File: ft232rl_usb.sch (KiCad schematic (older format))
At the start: 23 parts, among them J1 USB, P10 CONN_2, U1 FT232RL, U2 LM1117

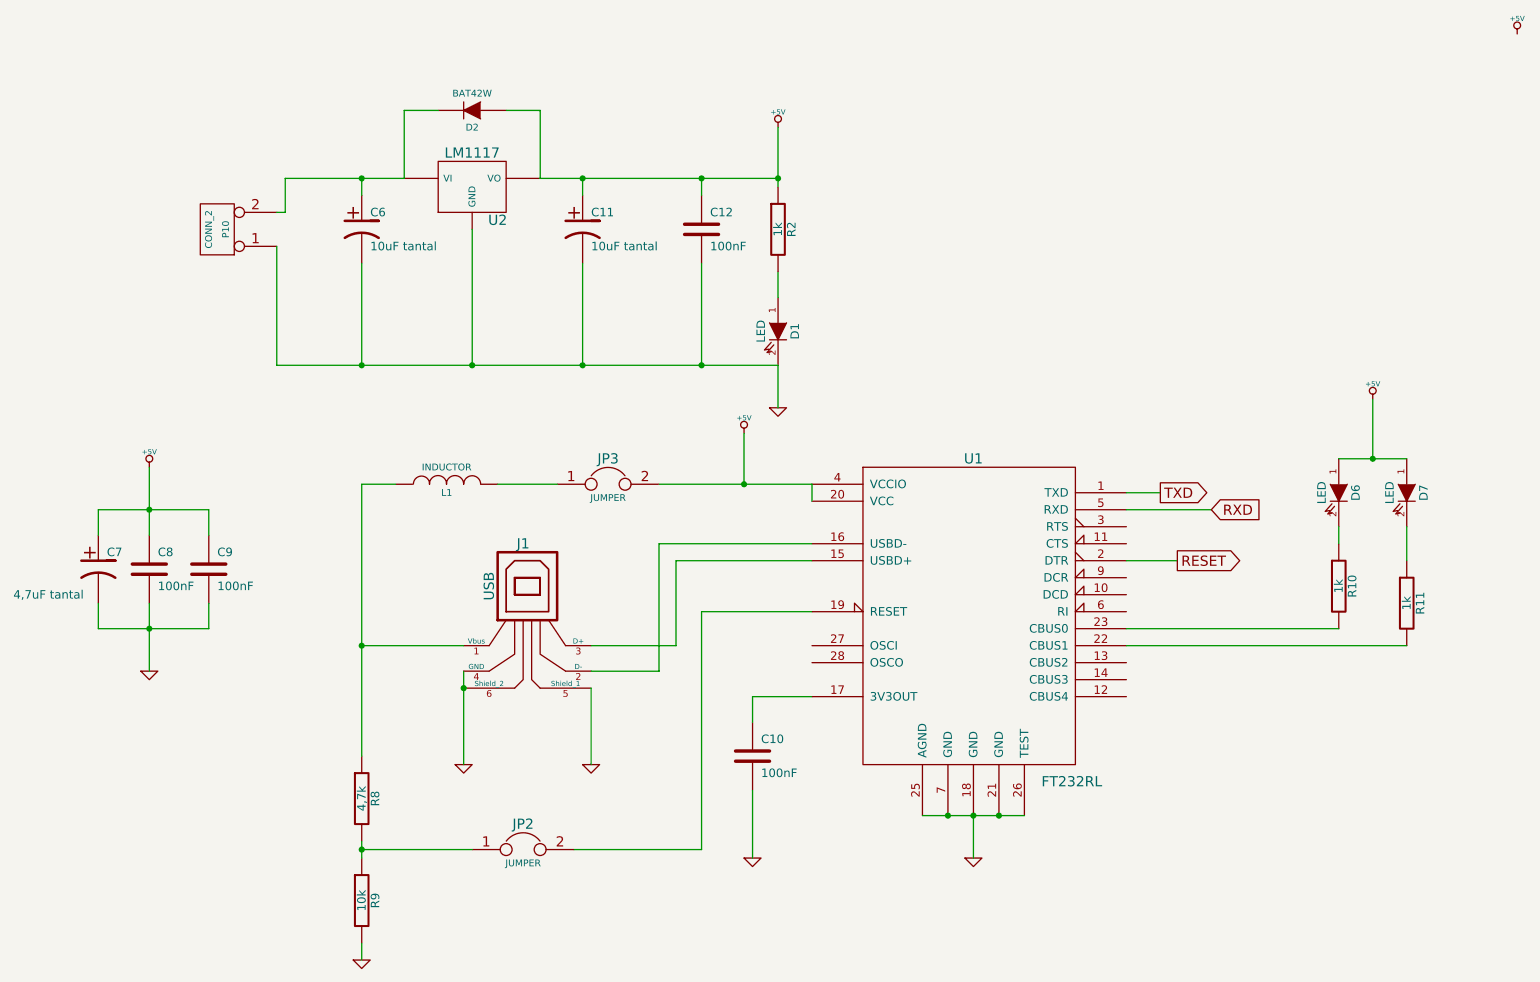
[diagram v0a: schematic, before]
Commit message: - Second version of the board - Added README for github
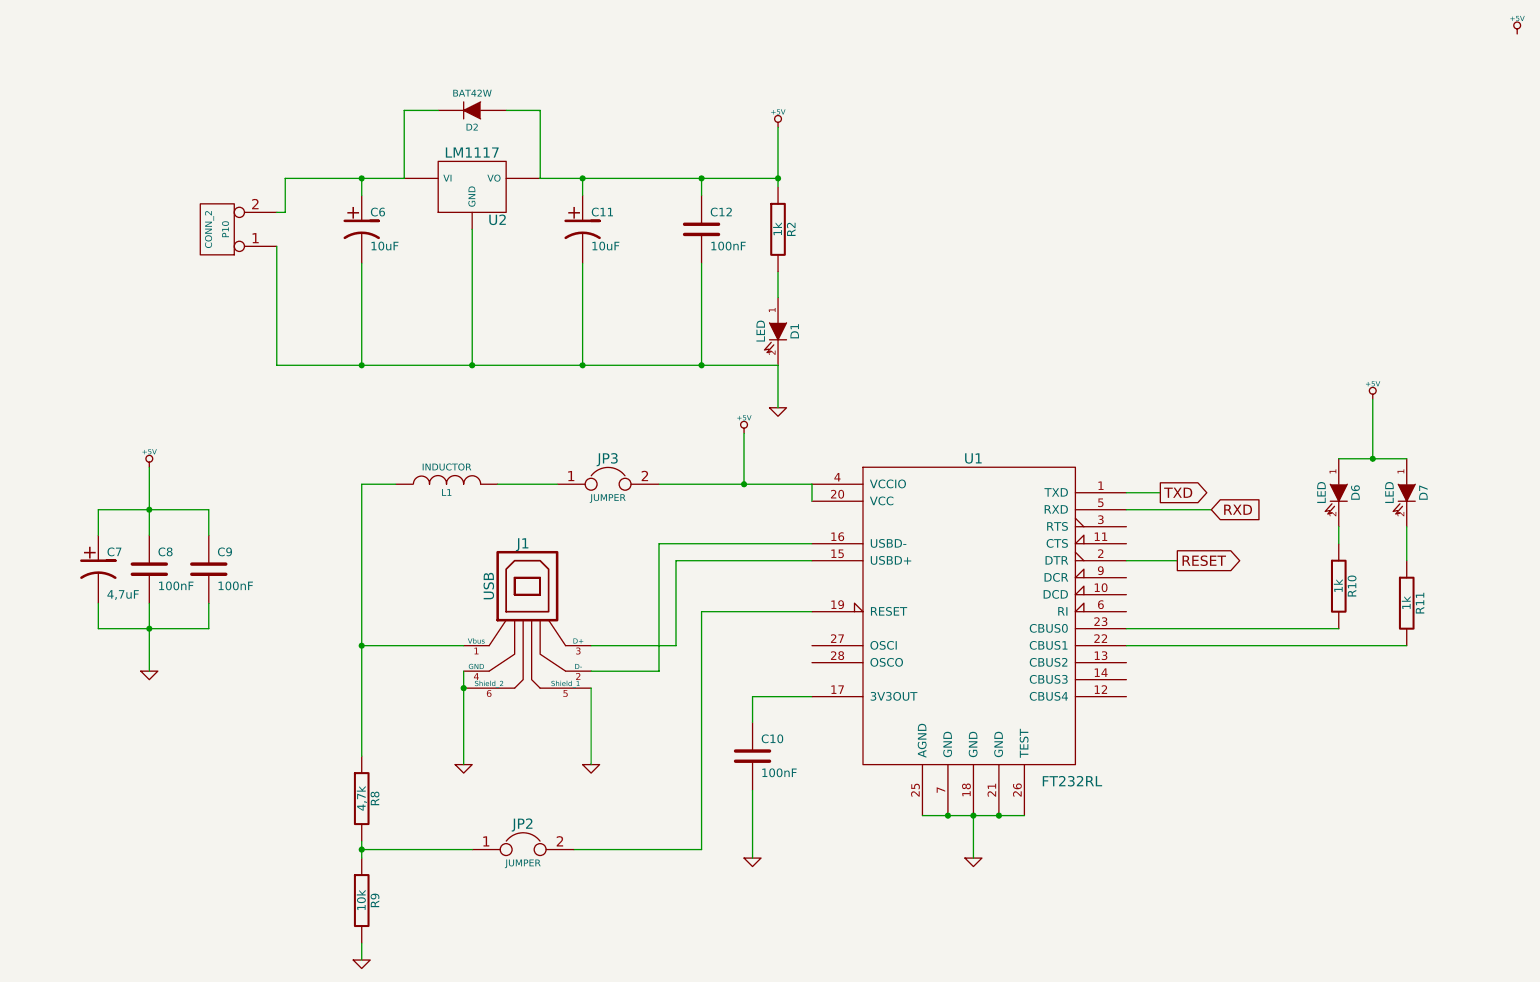
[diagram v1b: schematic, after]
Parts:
- C11, C6: value 10uF tantal -> 10uF
- C7: value 4,7uF tantal -> 4,7uF
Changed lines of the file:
@@
-EESchema Schematic File Version 2  date Sun 09 Dec 2012 11:53:08 PM CET
+EESchema Schematic File Version 2  date Thu 13 Dec 2012 04:01:05 PM CET
 LIBS:power
 LIBS:device
@@
 Sheet 2 2
 Title ""
-Date "9 dec 2012"
+Date "13 dec 2012"
 Rev ""
 Comp ""
@@
 $EndComp
 $Comp
-L GND #PWR013
+L GND #PWR015
 U 1 1 4F9D8FC2
 P 4700 4600
-F 0 "#PWR013" H 4700 4600 30  0001 C CNN
+F 0 "#PWR015" H 4700 4600 30  0001 C CNN
 F 1 "GND" H 4700 4530 30  0001 C CNN
 	1    4700 4600
@@
 P 1800 3450
 F 0 "C7" H 1850 3550 50  0000 L CNN
-F 1 "4,7uF tantal" H 1300 3300 50  0000 L CNN
+F 1 "4,7uF" H 1850 3300 50  0000 L CNN
 	1    1800 3450
 	1    0    0    -1
 $EndComp
 $Comp
-L GND #PWR014
+L GND #PWR016
 U 1 1 4F9D9229
 P 2100 4050
-F 0 "#PWR014" H 2100 4050 30  0001 C CNN
+F 0 "#PWR016" H 2100 4050 30  0001 C CNN
 F 1 "GND" H 2100 3980 30  0001 C CNN
 	1    2100 4050
@@
 $EndComp
 $Comp
-L +5V #PWR015
+L +5V #PWR017
 U 1 1 4F9D92D1
 P 2100 2850
-F 0 "#PWR015" H 2100 2940 20  0001 C CNN
+F 0 "#PWR017" H 2100 2940 20  0001 C CNN
 F 1 "+5V" H 2100 2940 30  0000 C CNN
 	1    2100 2850
@@
 $EndComp
 $Comp
-L +5V #PWR016
+L +5V #PWR018
 U 1 1 4F9D92E0
 P 5600 2650
-F 0 "#PWR016" H 5600 2740 20  0001 C CNN
+F 0 "#PWR018" H 5600 2740 20  0001 C CNN
 F 1 "+5V" H 5600 2740 30  0000 C CNN
 	1    5600 2650
@@
 $EndComp
 $Comp
-L GND #PWR017
+L GND #PWR019
 U 1 1 4F9D92EF
 P 3950 4600
-F 0 "#PWR017" H 3950 4600 30  0001 C CNN
+F 0 "#PWR019" H 3950 4600 30  0001 C CNN
 F 1 "GND" H 3950 4530 30  0001 C CNN
 	1    3950 4600
@@
 $EndComp
 $Comp
-L GND #PWR018
+L GND #PWR020
 U 1 1 4F9D9414
 P 6950 5150
-F 0 "#PWR018" H 6950 5150 30  0001 C CNN
+F 0 "#PWR020" H 6950 5150 30  0001 C CNN
 F 1 "GND" H 6950 5080 30  0001 C CNN
 	1    6950 5150
@@
 $EndComp
 $Comp
-L GND #PWR019
+L GND #PWR021
 U 1 1 4F9D9739
 P 3350 5750
-F 0 "#PWR019" H 3350 5750 30  0001 C CNN
+F 0 "#PWR021" H 3350 5750 30  0001 C CNN
 F 1 "GND" H 3350 5680 30  0001 C CNN
 	1    3350 5750
@@
 $EndComp
 $Comp
-L GND #PWR020
+L GND #PWR022
 U 1 1 4F9D9860
 P 5650 5150
-F 0 "#PWR020" H 5650 5150 30  0001 C CNN
+F 0 "#PWR022" H 5650 5150 30  0001 C CNN
 F 1 "GND" H 5650 5080 30  0001 C CNN
 	1    5650 5150
@@
 $EndComp
 $Comp
-L +5V #PWR021
+L +5V #PWR023
 U 1 1 4F9D9CC7
 P 9300 2450
-F 0 "#PWR021" H 9300 2540 20  0001 C CNN
+F 0 "#PWR023" H 9300 2540 20  0001 C CNN
 F 1 "+5V" H 9300 2540 30  0000 C CNN
 	1    9300 2450
@@
 P 3350 1450
 F 0 "C6" H 3400 1550 50  0000 L CNN
-F 1 "10uF tantal" H 3400 1350 50  0000 L CNN
+F 1 "10uF" H 3400 1350 50  0000 L CNN
 	1    3350 1450
 	1    0    0    -1
@@
 P 4650 1450
 F 0 "C11" H 4700 1550 50  0000 L CNN
-F 1 "10uF tantal" H 4700 1350 50  0000 L CNN
+F 1 "10uF" H 4700 1350 50  0000 L CNN
 	1    4650 1450
 	1    0    0    -1
@@
 Connection ~ 3350 3900
 Wire Wire Line
-	3350 4550 3350 3900
-Wire Wire Line
-	3350 3900 3350 2950
+	3350 2950 3350 4550
 Wire Wire Line
 	8150 3400 7850 3400
@@
 	9300 2800 9300 2450
 Wire Wire Line
-	9100 2800 9300 2800
-Wire Wire Line
-	9300 2800 9500 2800
+	9100 2800 9500 2800
 Wire Wire Line
 	9100 3300 9100 3200
@@
 Connection ~ 3350 5100
 Wire Wire Line
-	3350 5050 3350 5100
-Wire Wire Line
-	3350 5100 3350 5150
+	3350 5050 3350 5150
 Wire Wire Line
 	5350 3700 5350 5100
@@
 Connection ~ 2100 3800
 Wire Wire Line
-	1800 3800 2100 3800
-Wire Wire Line
-	2100 3800 2450 3800
-Wire Wire Line
-	2450 3250 2450 3100
-Wire Wire Line
-	2450 3100 2100 3100
-Wire Wire Line
-	2100 3100 1800 3100
+	1800 3800 2450 3800
+Wire Wire Line
+	2450 3100 2450 3250
+Wire Wire Line
+	1800 3100 2450 3100
 Wire Wire Line
 	6950 4900 6950 5150
@@
 Connection ~ 6800 4900
 Wire Wire Line
-	6650 4900 6800 4900
-Wire Wire Line
-	6800 4900 6950 4900
-Wire Wire Line
-	6950 4900 7100 4900
-Wire Wire Line
-	7100 4900 7250 4900
+	6650 4900 7250 4900
 Wire Wire Line
 	5600 2950 5600 2650
@@
 	1800 3800 1800 3650
 Wire Wire Line
-	2100 3650 2100 3800
-Wire Wire Line
-	2100 3800 2100 4050
+	2100 3650 2100 4050
 Connection ~ 2100 3100
 Wire Wire Line
 	1800 3100 1800 3250
 Wire Wire Line
-	2100 2850 2100 3100
-Wire Wire Line
-	2100 3100 2100 3250
+	2100 2850 2100 3250
 Wire Wire Line
 	3350 3900 3950 3900
@@
 	4700 4600 4700 4150
 Wire Wire Line
-	3950 4050 3950 4150
-Wire Wire Line
-	3950 4150 3950 4600
-Wire Wire Line
-	6000 3050 6000 2950
+	3950 4050 3950 4600
+Wire Wire Line
+	6000 2950 6000 3050
 Wire Wire Line
 	3350 2950 3550 2950
 Wire Wire Line
-	6000 2950 5600 2950
-Wire Wire Line
-	5600 2950 5100 2950
+	5100 2950 6000 2950
 Connection ~ 5600 2950
 Wire Wire Line
@@
 Connection ~ 4650 1150
 Wire Wire Line
-	4000 1450 4000 2250
+	4000 2250 4000 1450
 Wire Wire Line
 	3350 1250 3350 1150
 Wire Wire Line
-	3600 1150 3350 1150
-Wire Wire Line
-	3350 1150 2900 1150
+	2900 1150 3600 1150
 Wire Wire Line
 	4650 1250 4650 1150
@@
 	5350 1150 5350 1250
 Wire Wire Line
-	5350 1650 5350 2250
+	5350 2250 5350 1650
 Wire Wire Line
 	3350 1650 3350 2250
 Wire Wire Line
-	4650 1650 4650 2250
+	4650 2250 4650 1650
 Connection ~ 5350 1150
 $Comp
@@
 $EndComp
 Wire Wire Line
-	4400 1150 4650 1150
-Wire Wire Line
-	4650 1150 5350 1150
-Wire Wire Line
-	5350 1150 5800 1150
-Wire Wire Line
-	5800 850  5800 1150
-Wire Wire Line
-	5800 1150 5800 1200
+	4400 1150 5800 1150
+Wire Wire Line
+	5800 850  5800 1200
 Wire Wire Line
 	5800 1850 5800 1700
 Connection ~ 5800 1150
 $Comp
-L +5V #PWR022
+L +5V #PWR024
 U 1 1 50C4B5BF
 P 5800 850
-F 0 "#PWR022" H 5800 940 20  0001 C CNN
+F 0 "#PWR024" H 5800 940 20  0001 C CNN
 F 1 "+5V" H 5800 940 30  0000 C CNN
 	1    5800 850
@@
 $EndComp
 Wire Wire Line
-	2850 2250 3350 2250
-Wire Wire Line
-	3350 2250 4000 2250
-Wire Wire Line
-	4000 2250 4650 2250
-Wire Wire Line
-	4650 2250 5350 2250
-Wire Wire Line
-	5350 2250 5800 2250
+	2850 2250 5800 2250
 Connection ~ 3350 2250
 Connection ~ 4000 2250
@@
 Connection ~ 5350 2250
 $Comp
-L GND #PWR023
+L GND #PWR025
 U 1 1 50C4B798
 P 5800 2500
-F 0 "#PWR023" H 5800 2500 30  0001 C CNN
+F 0 "#PWR025" H 5800 2500 30  0001 C CNN
 F 1 "GND" H 5800 2430 30  0001 C CNN
 	1    5800 2500
@@
 $EndComp
 $Comp
-L +5V #PWR024
+L +5V #PWR026
 U 1 1 50C4BDF6
 P 10150 300
-F 0 "#PWR024" H 10150 390 20  0001 C CNN
+F 0 "#PWR026" H 10150 390 20  0001 C CNN
 F 1 "+5V" H 10150 390 30  0000 C CNN
 	1    10150 300
@@
 	4400 750  4200 750
 Wire Wire Line
-	3600 750  3600 1150
+	3600 1150 3600 750
 Wire Wire Line
 	3600 750  3800 750

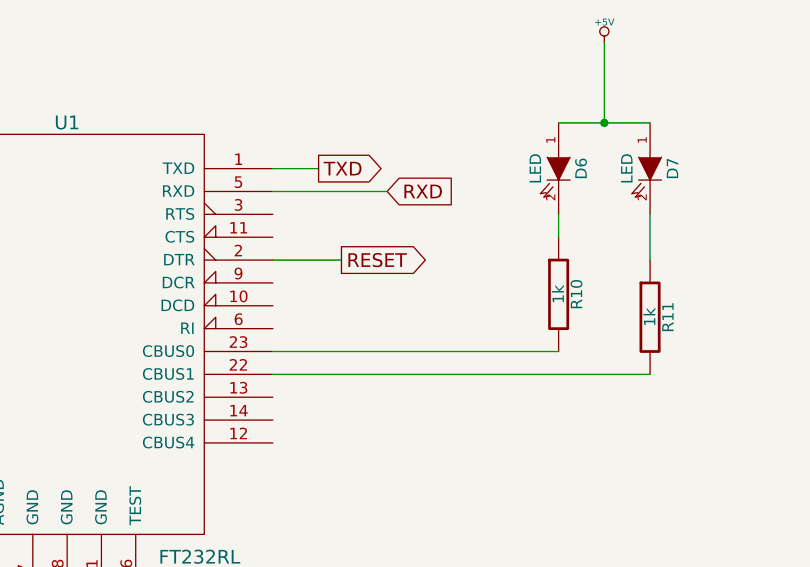
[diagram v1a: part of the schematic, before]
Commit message: Added list of known bugs on 1.0 Fixed the bugs and incremented version to 1.1
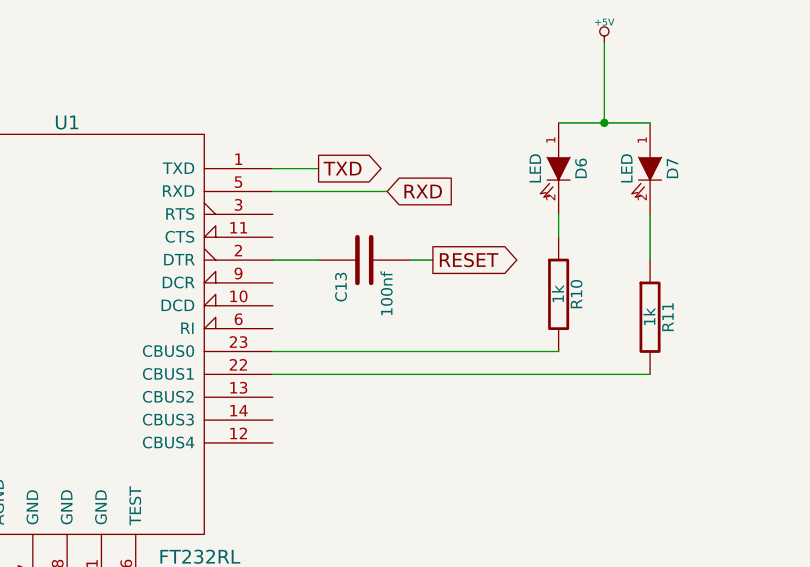
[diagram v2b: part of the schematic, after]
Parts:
- added C13: 100nf, symbol C
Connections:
- net RESET: now also C13.2; no longer U1.2 (DTR)
- new net: C13.1, U1.2 (DTR)
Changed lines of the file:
@@
-EESchema Schematic File Version 2  date Thu 13 Dec 2012 04:01:05 PM CET
+EESchema Schematic File Version 2  date Thu 10 Jan 2013 10:06:40 AM CET
 LIBS:power
 LIBS:device
@@
 encoding utf-8
 Sheet 2 2
-Title ""
-Date "13 dec 2012"
-Rev ""
+Title "Kaboard"
+Date "10 jan 2013"
+Rev "1.1"
 Comp ""
 Comment1 ""
@@
 	0    -1   -1   0
 $EndComp
-Text GLabel 8150 3400 2    60   Output ~ 0
+Text GLabel 8550 3400 2    60   Output ~ 0
 RESET
 $Comp
@@
 $EndComp
 $Comp
-L GND #PWR015
+L GND #PWR19
 U 1 1 4F9D8FC2
 P 4700 4600
-F 0 "#PWR015" H 4700 4600 30  0001 C CNN
+F 0 "#PWR19" H 4700 4600 30  0001 C CNN
 F 1 "GND" H 4700 4530 30  0001 C CNN
 	1    4700 4600
@@
 $EndComp
 $Comp
-L GND #PWR016
+L GND #PWR16
 U 1 1 4F9D9229
 P 2100 4050
-F 0 "#PWR016" H 2100 4050 30  0001 C CNN
+F 0 "#PWR16" H 2100 4050 30  0001 C CNN
 F 1 "GND" H 2100 3980 30  0001 C CNN
 	1    2100 4050
@@
 $EndComp
 $Comp
-L +5V #PWR017
+L +5V #PWR15
 U 1 1 4F9D92D1
 P 2100 2850
-F 0 "#PWR017" H 2100 2940 20  0001 C CNN
+F 0 "#PWR15" H 2100 2940 20  0001 C CNN
 F 1 "+5V" H 2100 2940 30  0000 C CNN
 	1    2100 2850
@@
 $EndComp
 $Comp
-L +5V #PWR018
+L +5V #PWR20
 U 1 1 4F9D92E0
 P 5600 2650
-F 0 "#PWR018" H 5600 2740 20  0001 C CNN
+F 0 "#PWR20" H 5600 2740 20  0001 C CNN
 F 1 "+5V" H 5600 2740 30  0000 C CNN
 	1    5600 2650
@@
 $EndComp
 $Comp
-L GND #PWR019
+L GND #PWR18
 U 1 1 4F9D92EF
 P 3950 4600
-F 0 "#PWR019" H 3950 4600 30  0001 C CNN
+F 0 "#PWR18" H 3950 4600 30  0001 C CNN
 F 1 "GND" H 3950 4530 30  0001 C CNN
 	1    3950 4600
@@
 $EndComp
 $Comp
-L GND #PWR020
+L GND #PWR24
 U 1 1 4F9D9414
 P 6950 5150
-F 0 "#PWR020" H 6950 5150 30  0001 C CNN
+F 0 "#PWR24" H 6950 5150 30  0001 C CNN
 F 1 "GND" H 6950 5080 30  0001 C CNN
 	1    6950 5150
@@
 $EndComp
 $Comp
-L GND #PWR021
+L GND #PWR17
 U 1 1 4F9D9739
 P 3350 5750
-F 0 "#PWR021" H 3350 5750 30  0001 C CNN
+F 0 "#PWR17" H 3350 5750 30  0001 C CNN
 F 1 "GND" H 3350 5680 30  0001 C CNN
 	1    3350 5750
@@
 $EndComp
 $Comp
-L GND #PWR022
+L GND #PWR21
 U 1 1 4F9D9860
 P 5650 5150
-F 0 "#PWR022" H 5650 5150 30  0001 C CNN
+F 0 "#PWR21" H 5650 5150 30  0001 C CNN
 F 1 "GND" H 5650 5080 30  0001 C CNN
 	1    5650 5150
@@
 $EndComp
 $Comp
-L +5V #PWR023
+L +5V #PWR25
 U 1 1 4F9D9CC7
 P 9300 2450
-F 0 "#PWR023" H 9300 2540 20  0001 C CNN
+F 0 "#PWR25" H 9300 2540 20  0001 C CNN
 F 1 "+5V" H 9300 2540 30  0000 C CNN
 	1    9300 2450
@@
 Wire Wire Line
 	3350 2950 3350 4550
-Wire Wire Line
-	8150 3400 7850 3400
 Connection ~ 9300 2800
 Wire Wire Line
@@
 Connection ~ 5800 1150
 $Comp
-L +5V #PWR024
+L +5V #PWR22
 U 1 1 50C4B5BF
 P 5800 850
-F 0 "#PWR024" H 5800 940 20  0001 C CNN
+F 0 "#PWR22" H 5800 940 20  0001 C CNN
 F 1 "+5V" H 5800 940 30  0000 C CNN
 	1    5800 850
@@
 Connection ~ 5350 2250
 $Comp
-L GND #PWR025
+L GND #PWR23
 U 1 1 50C4B798
 P 5800 2500
-F 0 "#PWR025" H 5800 2500 30  0001 C CNN
+F 0 "#PWR23" H 5800 2500 30  0001 C CNN
 F 1 "GND" H 5800 2430 30  0001 C CNN
 	1    5800 2500
@@
 $EndComp
 $Comp
-L +5V #PWR026
+L +5V #PWR26
 U 1 1 50C4BDF6
 P 10150 300
-F 0 "#PWR026" H 10150 390 20  0001 C CNN
+F 0 "#PWR26" H 10150 390 20  0001 C CNN
 F 1 "+5V" H 10150 390 30  0000 C CNN
 	1    10150 300
@@
 Wire Wire Line
 	3600 750  3800 750
+$Comp
+L C C13
+U 1 1 50EE8982
+P 8250 3400
+F 0 "C13" H 8300 3500 50  0000 L CNN
+F 1 "100nf" H 8300 3300 50  0000 L CNN
+	1    8250 3400
+	0    -1   1    0
+$EndComp
+Wire Wire Line
+	7850 3400 8050 3400
+Wire Wire Line
+	8450 3400 8550 3400
 $EndSCHEMATC

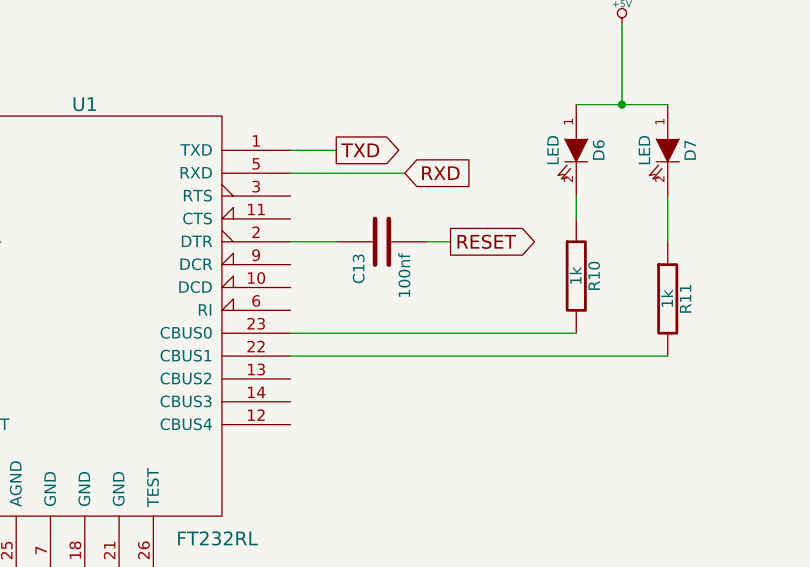
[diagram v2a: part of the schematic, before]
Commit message: Small fixed to make the reset circut more reliable
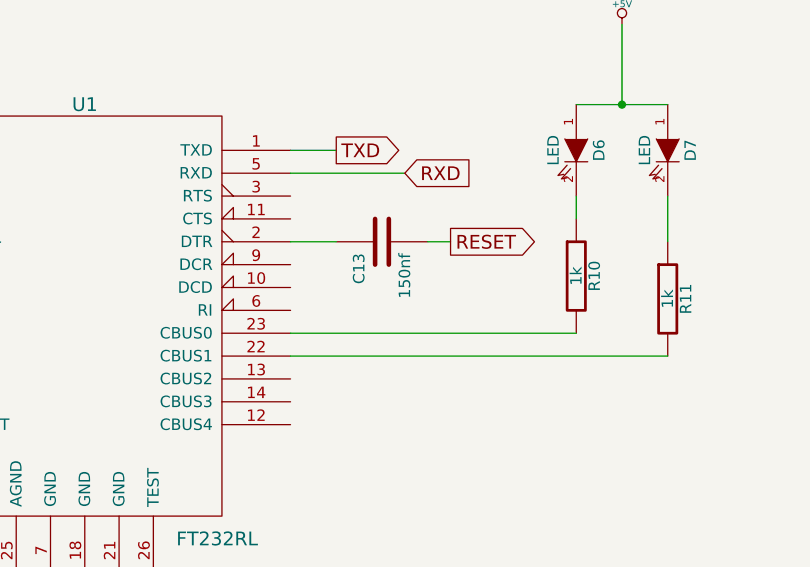
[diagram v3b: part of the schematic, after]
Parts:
- C13: value 100nf -> 150nf
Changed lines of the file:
@@
-EESchema Schematic File Version 2  date Thu 10 Jan 2013 10:06:40 AM CET
+EESchema Schematic File Version 2  date Thu 17 Jan 2013 01:01:30 PM CET
 LIBS:power
 LIBS:device
@@
 Sheet 2 2
 Title "Kaboard"
-Date "10 jan 2013"
+Date "17 jan 2013"
 Rev "1.1"
 Comp ""
@@
 P 8250 3400
 F 0 "C13" H 8300 3500 50  0000 L CNN
-F 1 "100nf" H 8300 3300 50  0000 L CNN
+F 1 "150nf" H 8300 3300 50  0000 L CNN
 	1    8250 3400
 	0    -1   1    0
